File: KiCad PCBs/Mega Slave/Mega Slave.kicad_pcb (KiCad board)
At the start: 2 copper layers, 0 parts

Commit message: Mega Slave WIP
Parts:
- added C1: 4.7uF, A10 KiCad Libraries:C0805, F.Cu at (144.8, 91.4)
- added C10: 1uF, A10 KiCad Libraries:C0402, F.Cu at (136.4, 102.2)
- added C11: 15pF, A10 KiCad Libraries:C0402, F.Cu at (147.3, 86.4)
- added C12: 15pF, A10 KiCad Libraries:C0402, F.Cu at (149.6, 84.1)
- added C13: 100nF, A10 KiCad Libraries:C0402, F.Cu at (167.6, 101.0)
- added C14: 100nF, A10 KiCad Libraries:C0402, F.Cu at (140.3, 104.1)
- added C2: 1uF, A10 KiCad Libraries:C0402, F.Cu at (165.7, 90.2)
- added C3: 1uF, A10 KiCad Libraries:C0402, F.Cu at (168.9, 99.7)
- added C4: 1uF, A10 KiCad Libraries:C0402, F.Cu at (161.9, 107.3)
- added C5: 1uF, A10 KiCad Libraries:C0402, F.Cu at (148.2, 103.9)
- added C6: 1uF, A10 KiCad Libraries:C0402, F.Cu at (154.3, 84.5)
- added C7: 47uF, Capacitor_SMD:CP_Elec_5x5.4, F.Cu at (119.4, 89.5)
- added C8: 10uF, A10 KiCad Libraries:C0402, F.Cu at (114.3, 91.4)
- added C9: 1uF, A10 KiCad Libraries:C0402, F.Cu at (114.9, 83.2)
- added D1: LED, LED_SMD:LED_0603_1608Metric, F.Cu at (151.8, 114.3)
- added D2: LED, LED_SMD:LED_0603_1608Metric, F.Cu at (134.6, 88.9)
- added H1: MountingHole, MountingHole:MountingHole_3.2mm_M3, F.Cu at (95.2, 69.2)
- added H2: MountingHole, MountingHole:MountingHole_3.2mm_M3, F.Cu at (190.5, 69.2)
- added H3: MountingHole, MountingHole:MountingHole_3.2mm_M3, F.Cu at (95.2, 123.8)
- added H4: MountingHole, MountingHole:MountingHole_3.2mm_M3, F.Cu at (190.5, 123.8)
- added J1: AVR-ISP-6, Connector_PinHeader_2.54mm:PinHeader_2x03_P2.54mm_Vertical, F.Cu at (169.5, 87.0)
- added J10: Screw_Terminal_01x02, A10 KiCad Libraries:CONN-TH_XY308-2.54-2P, F.Cu at (133.4, 123.8)
- added J11: Screw_Terminal_01x02, A10 KiCad Libraries:CONN-TH_XY308-2.54-2P, F.Cu at (127.6, 123.8)
- added J12: Screw_Terminal_01x02, A10 KiCad Libraries:CONN-TH_XY308-2.54-2P, F.Cu at (121.9, 123.8)
- added J13: Screw_Terminal_01x02, A10 KiCad Libraries:CONN-TH_XY308-2.54-2P, F.Cu at (116.2, 123.8)
- added J14: Screw_Terminal_01x02, A10 KiCad Libraries:CONN-TH_XY308-2.54-2P, F.Cu at (110.5, 123.8)
- added J15: Screw_Terminal_01x02, A10 KiCad Libraries:CONN-TH_XY308-2.54-2P, F.Cu at (104.8, 123.8)
- added J16: Screw_Terminal_01x02, A10 KiCad Libraries:CONN-TH_XY308-2.54-2P, F.Cu at (110.5, 69.2)
- added J17: Screw_Terminal_01x02, A10 KiCad Libraries:CONN-TH_XY308-2.54-2P, F.Cu at (116.2, 69.2)
- added J18: Screw_Terminal_01x02, A10 KiCad Libraries:CONN-TH_XY308-2.54-2P, F.Cu at (121.9, 69.2)
- added J19: Screw_Terminal_01x02, A10 KiCad Libraries:CONN-TH_XY308-2.54-2P, F.Cu at (127.6, 69.2)
- added J2: Screw_Terminal_01x02, A10 KiCad Libraries:CONN-TH_XY308-2.54-2P, F.Cu at (179.1, 123.8)
- added J20: Screw_Terminal_01x02, A10 KiCad Libraries:CONN-TH_XY308-2.54-2P, F.Cu at (133.3, 69.2)
- added J21: Screw_Terminal_01x02, A10 KiCad Libraries:CONN-TH_XY308-2.54-2P, F.Cu at (139.1, 69.2)
- added J22: Screw_Terminal_01x02, A10 KiCad Libraries:CONN-TH_XY308-2.54-2P, F.Cu at (144.8, 69.2)
- added J23: Screw_Terminal_01x02, A10 KiCad Libraries:CONN-TH_XY308-2.54-2P, F.Cu at (150.5, 69.2)
- added J24: Screw_Terminal_01x02, A10 KiCad Libraries:CONN-TH_XY308-2.54-2P, F.Cu at (156.2, 69.2)
- added J25: Screw_Terminal_01x02, A10 KiCad Libraries:CONN-TH_XY308-2.54-2P, F.Cu at (161.9, 69.2)
- added J26: Screw_Terminal_01x02, A10 KiCad Libraries:CONN-TH_XY308-2.54-2P, F.Cu at (167.6, 69.2)
- added J27: Screw_Terminal_01x02, A10 KiCad Libraries:CONN-TH_XY308-2.54-2P, F.Cu at (173.4, 69.2)
- added J28: Screw_Terminal_01x02, A10 KiCad Libraries:CONN-TH_XY308-2.54-2P, F.Cu at (190.5, 76.2)
- added J29: Screw_Terminal_01x02, A10 KiCad Libraries:CONN-TH_XY308-2.54-2P, F.Cu at (190.5, 81.9)
- added J3: Screw_Terminal_01x02, A10 KiCad Libraries:CONN-TH_XY308-2.54-2P, F.Cu at (173.4, 123.8)
- added J30: Screw_Terminal_01x02, A10 KiCad Libraries:CONN-TH_XY308-2.54-2P, F.Cu at (190.5, 87.6)
- added J31: Screw_Terminal_01x02, A10 KiCad Libraries:CONN-TH_XY308-2.54-2P, F.Cu at (190.5, 93.3)
- added J32: Screw_Terminal_01x02, A10 KiCad Libraries:CONN-TH_XY308-2.54-2P, F.Cu at (190.5, 99.1)
- added J33: Screw_Terminal_01x02, A10 KiCad Libraries:CONN-TH_XY308-2.54-2P, F.Cu at (190.5, 104.8)
- added J34: Screw_Terminal_01x02, A10 KiCad Libraries:CONN-TH_XY308-2.54-2P, F.Cu at (190.5, 110.5)
- added J35: Screw_Terminal_01x02, A10 KiCad Libraries:CONN-TH_XY308-2.54-2P, F.Cu at (190.5, 116.2)
- added J36: Screw_Terminal_01x02, A10 KiCad Libraries:CONN-TH_XY308-2.54-2P, F.Cu at (95.2, 103.5)
- added J37: Screw_Terminal_01x02, A10 KiCad Libraries:CONN-TH_XY308-2.54-2P, F.Cu at (95.2, 76.8)
- added J38: Screw_Terminal_01x02, A10 KiCad Libraries:CONN-TH_XY308-2.54-2P, F.Cu at (103.5, 69.2)
- added J39: Conn_01x06_Female, Connector_PinSocket_2.54mm:PinSocket_1x06_P2.54mm_Vertical, F.Cu at (140.3, 107.3)
- added J4: Screw_Terminal_01x02, A10 KiCad Libraries:CONN-TH_XY308-2.54-2P, F.Cu at (167.6, 123.8)
- added J40: Screw_Terminal_01x02, A10 KiCad Libraries:CONN-TH_XY308-2.54-2P, F.Cu at (95.2, 116.2)
- added J41: Screw_Terminal_01x02, A10 KiCad Libraries:CONN-TH_XY308-2.54-2P, F.Cu at (95.2, 109.9)
- added J5: Screw_Terminal_01x02, A10 KiCad Libraries:CONN-TH_XY308-2.54-2P, F.Cu at (161.9, 123.8)
- added J6: Screw_Terminal_01x02, A10 KiCad Libraries:CONN-TH_XY308-2.54-2P, F.Cu at (156.2, 123.8)
- added J7: Screw_Terminal_01x02, A10 KiCad Libraries:CONN-TH_XY308-2.54-2P, F.Cu at (150.5, 123.8)
- added J8: Screw_Terminal_01x02, A10 KiCad Libraries:CONN-TH_XY308-2.54-2P, F.Cu at (144.8, 123.8)
- added J9: Screw_Terminal_01x02, A10 KiCad Libraries:CONN-TH_XY308-2.54-2P, F.Cu at (139.1, 123.8)
- added R1: 10K, Resistor_SMD:R_0805_2012Metric, F.Cu at (167.0, 85.7)
- added R2: 120R, Resistor_SMD:R_0805_2012Metric, F.Cu at (123.2, 95.2)
- added R3: 1K, Resistor_SMD:R_0805_2012Metric, F.Cu at (151.8, 110.5)
- added R4: 1.8K, Resistor_SMD:R_0805_2012Metric, F.Cu at (110.5, 94.6)
- added R5: 1.8K, Resistor_SMD:R_0805_2012Metric, F.Cu at (110.5, 85.7)
- added R6: 1K, Resistor_SMD:R_0805_2012Metric, F.Cu at (130.8, 88.9)
- added RJ1: RJ45-B-1*1, A10 KiCad Libraries:RJ45-TH_B-1-1, F.Cu at (100.3, 90.2)
- added SW1: SW_MEC_5E, A10 KiCad Libraries:SW-SMD_4P-L5.1-W5.1-P3.70-LS6.5-TL-2, F.Cu at (181.6, 69.2)
- added SW2: SW_DIP_x02, A10 KiCad Libraries:SW-SMD_DSHP02TSGER, F.Cu at (129.5, 97.8)
- added SW3: SW_DIP_x02, A10 KiCad Libraries:SW-SMD_DSHP02TSGER, F.Cu at (118.7, 108.6)
- added U1: ATmega2560-16A, Package_QFP:TQFP-100_14x14mm_P0.5mm, F.Cu at (156.8, 96.5)
- added U2: MAX487ESA+T, A10 KiCad Libraries:SOIC-8_L5.0-W4.0-P1.27-LS6.0-BL, F.Cu at (139.1, 97.8)
- added U3: AMS1117-5.0, Package_TO_SOT_SMD:SOT-223-3_TabPin2, F.Cu at (119.4, 81.3)
- added U4: ULN2003A, A10 KiCad Libraries:SOP-16_L10.0-W3.9-P1.27-LS6.0-BL, F.Cu at (108.0, 108.0)
- added Y1: Crystal_GND24, Crystal:Crystal_SMD_3225-4Pin_3.2x2.5mm, F.Cu at (150.5, 87.0)
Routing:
- net +12V: track 0.00 -> 77.0 mm
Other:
- board outline added: 102.9 x 62.2 mm
- board text added: "INPUT ← D13 → BACKLIGHT"
- board text added: "INPUT ← D4 → BACKLIGHT"
- board text added: "MISO"
- board text added: "OFF ← RS485 → ON"
- board text added: "OFF ← TERM → ON"
- board text added: "WarthogAtHome.com"

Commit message: Mega Slave Initial Routing
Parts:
- moved R1 11.2 mm to (177.4, 81.5), turned to 0 degrees
- moved C13 4.38 mm to (170.1, 97.3), turned to -135 degrees
- moved C3 3.93 mm to (168.4, 95.8), turned to 45 degrees
- moved C11 3.54 mm to (148.2, 89.8)
- moved C12 2.89 mm to (152.4, 83.2)
- moved C6 0.66 mm to (153.6, 84.4)
- moved C5 0.60 mm to (148.5, 103.4)
- moved Y1 0.59 mm to (150.3, 86.4)
- moved R2 0.57 mm to (122.9, 95.8)
- moved C4 0.43 mm to (161.7, 107.0)
- moved C2 0.30 mm to (165.5, 90.0)
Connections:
- U1 pad 13: D18 -> D16
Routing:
- net +5V: track 0.00 -> 122.9 mm, vias 0 -> 10
- net D4: track 0.00 -> 112.8 mm, vias 0 -> 4
- net TXD: track 0.00 -> 102.5 mm, vias 0 -> 6
- net RXD: track 0.00 -> 99.1 mm, vias 0 -> 4
- net D13: track 0.00 -> 92.3 mm, vias 0 -> 4
- net RESET: track 0.00 -> 74.2 mm, vias 0 -> 4
- net D31: track 0.00 -> 63.0 mm
- net D30: track 0.00 -> 61.8 mm, vias 0 -> 2
- net D32: track 0.00 -> 60.0 mm
- net D29: track 0.00 -> 59.3 mm, vias 0 -> 2
- net D33: track 0.00 -> 56.2 mm
- net D28: track 0.00 -> 56.1 mm, vias 0 -> 2
- net D27: track 0.00 -> 53.8 mm, vias 0 -> 2
- net D34: track 0.00 -> 52.9 mm
- net D26: track 0.00 -> 50.8 mm, vias 0 -> 2
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- added copper zone on F.Cu, net +5V
- added copper zone on B.Cu, net GND
- added copper zone on F.Cu, net GND
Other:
- board text removed: "MISO"

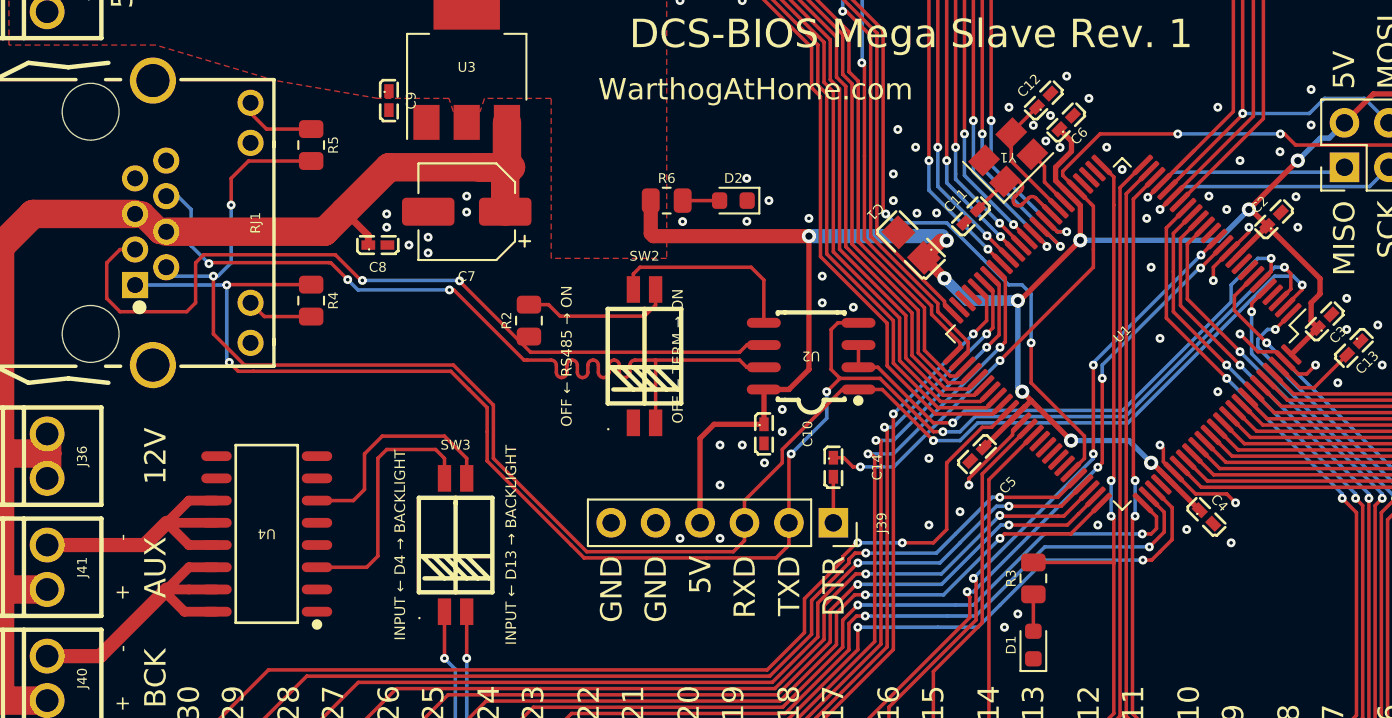
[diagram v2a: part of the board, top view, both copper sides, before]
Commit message: Mega Slave Completed
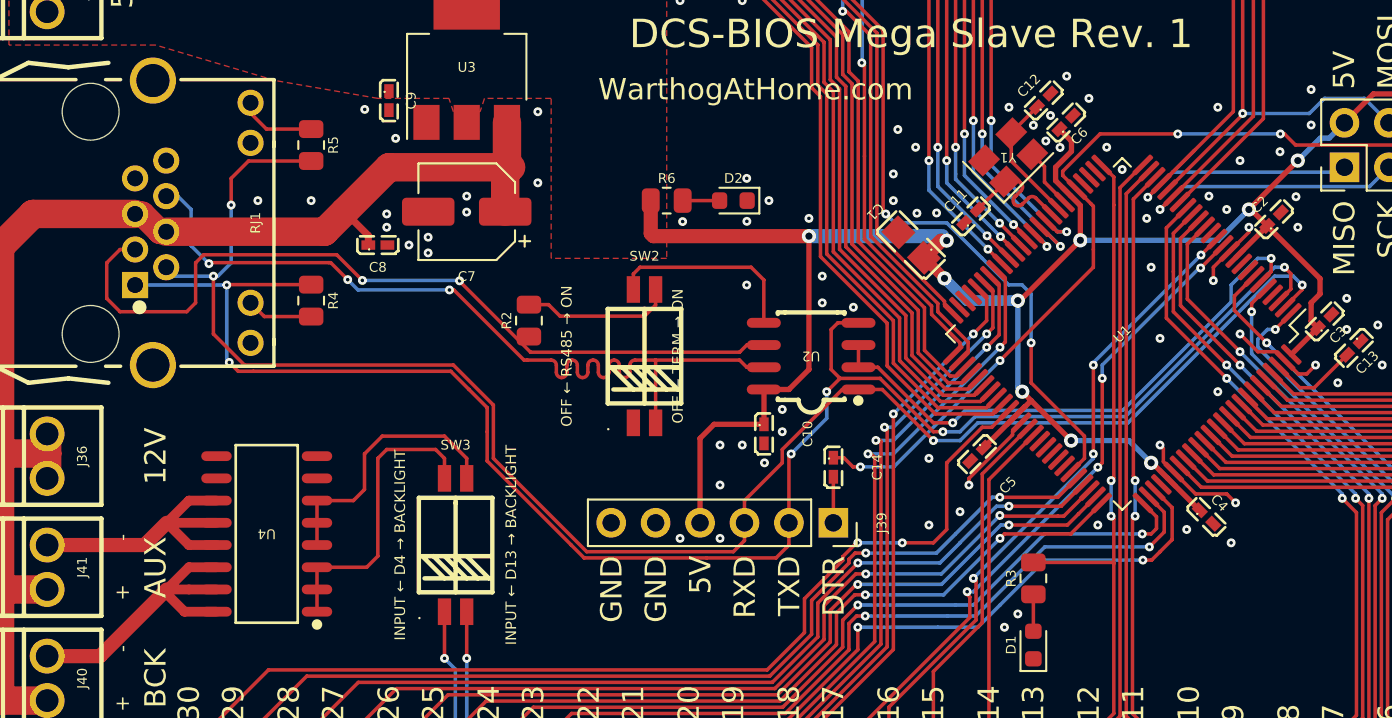
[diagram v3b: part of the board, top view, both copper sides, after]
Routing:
- net AUX_BASE: track 12.9 -> 15.5 mm
- net BACKLIGHT_BASE: track 14.7 -> 17.2 mm
- net +12V: track 77.0 -> 76.0 mm
- net TXD: track 102.5 -> 101.6 mm
- net GND: vias 86 -> 93
